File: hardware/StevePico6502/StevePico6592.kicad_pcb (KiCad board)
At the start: 2 copper layers, 112.4 x 101.6 mm, 29 parts, among them J1 Conn_01x16, J2 Conn_01x16, J3 Conn_02x16_Odd_Even, J4 Conn_01x01_Pin, SW1 SW_Push, SW2 SW_Push, U1 65CE02, U2 Pico, U3 74HC595, U4 W65C22NxP, U5 CY62256-70PC, U6 74HC00

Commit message: fixed bug with dual RAMSEL and no ROMSEL
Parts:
- U2: footprint Pi Pico:RPi_Pico_SMD_TH -> MCU_RaspberryPi_and_Boards:RPi_Pico_SMD_TH
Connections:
- U2 pad 10: /~{RAMSEL} -> /~{ROMSEL}
- U3 pad 13: /~{RAMSEL} -> /~{ROMSEL}
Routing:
- net /~{ROMSEL}: track 0.00 -> 52.0 mm, vias 0 -> 2
- net /~{RAMSEL}: track 120.1 -> 113.6 mm
- net /A14: track 135.2 -> 141.0 mm
- net /D1: track 155.2 -> 158.7 mm
- net /A7: track 159.9 -> 162.5 mm
- net GND: track 438.5 -> 440.5 mm
- net /~{IOSEL}: track 190.3 -> 191.5 mm
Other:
- board text added: "V082323 Has an error where GPIO5 and GPIO7 are both marked as ~{RAMSE}. To Fix: - cut the trace on the backside from pin 10 to the via which then connects to pin 7. - Pin 13 of U3 should be connected to ~{ROMSEL} not ~{RAMSEL} and will need to be cut and bodged. - Pin 20 of U5 should be connected to ~{RAMSE} with a bodge wire."

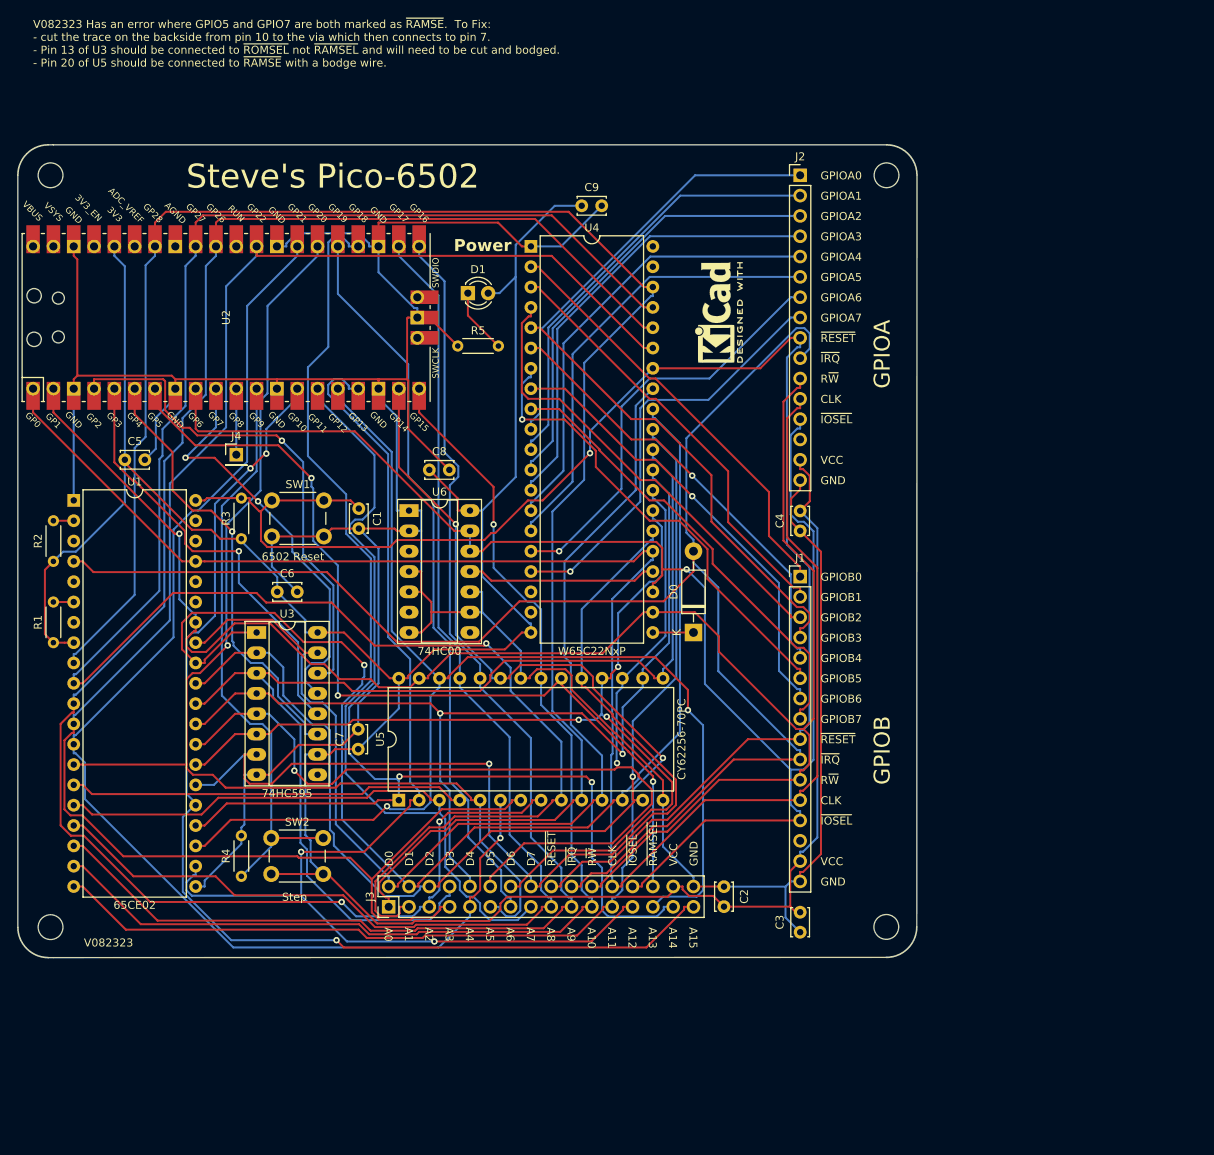
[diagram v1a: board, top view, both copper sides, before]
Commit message: V090323 - Removed Pico
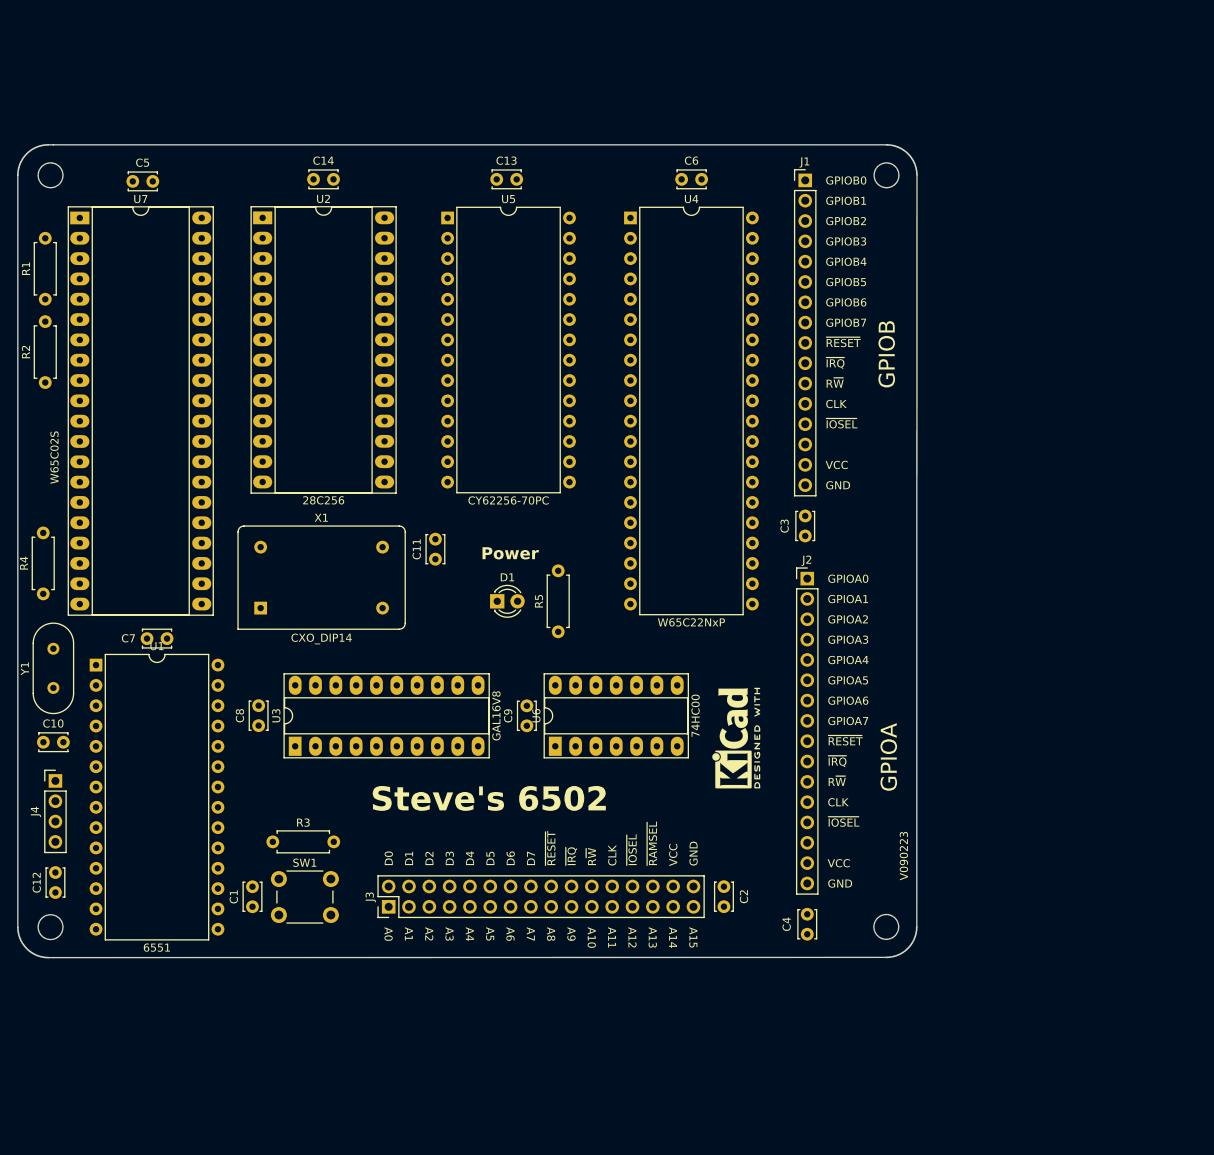
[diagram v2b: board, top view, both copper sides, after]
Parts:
- removed D0: SB140, Diode_THT:D_DO-41_SOD81_P10.16mm_Horizontal
- removed SW2: SW_Push, Button_Switch_THT:SW_PUSH_6mm
- added C10: 30pf, Capacitor_THT:C_Disc_D3.4mm_W2.1mm_P2.50mm, F.Cu at (52.1, 107.7)
- added C11: 1uF, Capacitor_THT:C_Disc_D3.4mm_W2.1mm_P2.50mm, F.Cu at (101.1, 84.8)
- added C12: 1uF, Capacitor_THT:C_Disc_D3.4mm_W2.1mm_P2.50mm, F.Cu at (53.6, 126.5)
- added C13: 1uF, Capacitor_THT:C_Disc_D3.4mm_W2.1mm_P2.50mm, F.Cu at (108.8, 37.3)
- added C14: 1uF, Capacitor_THT:C_Disc_D3.4mm_W2.1mm_P2.50mm, F.Cu at (85.9, 37.3)
- added U7: ~, Package_DIP:DIP-40_W15.24mm_Socket_LongPads, F.Cu at (56.6, 42.2)
- added X1: CXO_DIP14, Oscillator:Oscillator_DIP-14, F.Cu at (79.2, 90.9)
- added Y1: 1.8432, Crystal:Crystal_HC18-U_Vertical, F.Cu at (53.3, 100.9)
- J4: value Conn_01x01_Pin -> Conn_01x04; footprint Connector_PinHeader_2.54mm:PinHeader_1x01_P2.54mm_Vertical -> Connector_PinHeader_2.54mm:PinHeader_1x04_P2.54mm_Vertical
- R1, R2, R3, R4: footprint Resistor_THT:R_Axial_DIN0204_L3.6mm_D1.6mm_P5.08mm_Horizontal -> Resistor_THT:R_Axial_DIN0207_L6.3mm_D2.5mm_P7.62mm_Horizontal
- R5: value 1k -> 220; footprint Resistor_THT:R_Axial_DIN0204_L3.6mm_D1.6mm_P5.08mm_Horizontal -> Resistor_THT:R_Axial_DIN0207_L6.3mm_D2.5mm_P7.62mm_Horizontal
- U1: value 65CE02 -> 6551; footprint Package_DIP:DIP-40_W15.24mm -> Package_DIP:DIP-28_W15.24mm
- U2: value Pico -> 28C256; footprint MCU_RaspberryPi_and_Boards:RPi_Pico_SMD_TH -> Package_DIP:DIP-28_W15.24mm_Socket_LongPads
- U3: value 74HC595 -> GAL16V8; footprint Package_DIP:DIP-16_W7.62mm_Socket_LongPads -> Package_DIP:DIP-20_W7.62mm_Socket_LongPads
- moved U5 73.0 mm to (102.6, 42.2), turned to 0 degrees
- moved C6 72.2 mm to (131.9, 37.3)
- moved C9 65.4 mm to (112.5, 105.6), turned to 90 degrees
- moved REF** 53.3 mm to (138.7, 107.2)
- moved C1 51.5 mm to (78.2, 128.3), turned to 90 degrees
- moved C4 50.4 mm to (147.6, 129.2)
- moved J2 50.4 mm to (147.6, 87.2)
- moved J1 49.5 mm to (147.3, 37.5)
- moved C3 49.5 mm to (147.3, 79.4)
- moved SW1 47.3 mm to (81.5, 124.8)
- moved J4 46.6 mm to (53.6, 112.5)
- moved R4 43.1 mm to (52.1, 89.2)
- moved R1 42.9 mm to (52.3, 52.3)
- moved D1 38.7 mm to (108.8, 90.1)
- moved C8 38.4 mm to (79.0, 105.6), turned to 90 degrees
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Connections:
- J4 pad 1: Net-(J4-Pin_1) -> /RXD
- R1 pad 2: Net-(U1-~{NMI}) -> Net-(U7-RDY)
- R2 pad 2: Net-(U1-RDY) -> Net-(U7-NMIB)
- R4 pad 1: Net-(U2-GPIO9) -> Net-(U1-XTAL2)
- R4 pad 2: GND -> Net-(U1-XTAL1)
- U1 pad 10: /A1 -> /TXD
- U1 pad 11: /A2 -> unconnected-(U1-~{DTR}-Pad11)
- U1 pad 12: /A3 -> /RXD
- U1 pad 13: /A4 -> /A0
- U1 pad 14: /A5 -> /A1
- U1 pad 15: /A6 -> VCC
- U1 pad 16: /A7 -> unconnected-(U1-~{DCD}-Pad16)
- U1 pad 17: /A8 -> unconnected-(U1-~{DSR}-Pad17)
- U1 pad 18: /A9 -> /D0
- U1 pad 19: /A10 -> /D1
- U1 pad 2: Net-(U1-RDY) -> /UARTSEL
- U1 pad 20: /A11 -> /D2
- U1 pad 21: GND -> /D3
- U1 pad 22: /A12 -> /D4
- U1 pad 23: /A13 -> /D5
- U1 pad 24: /A14 -> /D6
- U1 pad 25: /A15 -> /D7
- U1 pad 26: /D7 -> unconnected-(U1-~{IRQ}-Pad26)
- U1 pad 27: /D6 -> /CLK
- U1 pad 28: /D5 -> /R~{W}
- U1 pad 3: unconnected-(U1-ϕ1-Pad3) -> /~{UARTSEL}
- U1 pad 4: /~{IRQ} -> /~{RESET}
- U1 pad 6: Net-(U1-~{NMI}) -> Net-(U1-XTAL1)
- U1 pad 7: unconnected-(U1-SYNC-Pad7) -> Net-(U1-XTAL2)
- U1 pad 8: VCC -> unconnected-(U1-~{RTS}-Pad8)
- U1 pad 9: /A0 -> unconnected-(U1-~{CTS}-Pad9)
- U2 pad 1: /CLK -> /A14
- U2 pad 10: /~{ROMSEL} -> /A0
- U2 pad 11: Net-(J4-Pin_1) -> /D0
- U2 pad 12: Net-(U2-GPIO9) -> /D1
- U2 pad 13: GND -> /D2
- U2 pad 14: /A15 -> GND
- U2 pad 15: /A14 -> /D3
- U2 pad 16: /A13 -> /D4
- U2 pad 17: /A12 -> /D5
- U2 pad 18: GND -> /D6
- U2 pad 19: /A11 -> /D7
- U2 pad 2: /R~{W} -> /A12
- U2 pad 20: /A10 -> /~{ROMSEL}
- U2 pad 21: /A9 -> /A10
- U2 pad 22: /A8 -> /R~{W}
- U2 pad 23: GND -> /A11
- U2 pad 24: /A7 -> /A9
- U2 pad 25: /A6 -> /A8
- U2 pad 26: /A5 -> /A13
- U2 pad 27: /A4 -> VCC
- U2 pad 28: GND -> VCC
- U2 pad 3: GND -> /A7
- U2 pad 4: Net-(U2-GPIO2) -> /A6
- U2 pad 5: Net-(U2-GPIO3) -> /A5
- U2 pad 6: Net-(U2-GPIO4) -> /A4
- U2 pad 7: /~{RAMSEL} -> /A3
- U2 pad 8: GND -> /A2
- U2 pad 9: /~{IOSEL} -> /A1
- U3 pad 1: /D1 -> /A15
- U3 pad 10: VCC -> GND
- U3 pad 11: Net-(U2-GPIO4) -> unconnected-(U3-I10/~{OE}-Pad11)
- U3 pad 12: Net-(U2-GPIO3) -> unconnected-(U3-IO8-Pad12)
- U3 pad 13: /~{ROMSEL} -> unconnected-(U3-IO7-Pad13)
- U3 pad 14: Net-(U2-GPIO2) -> unconnected-(U3-IO6-Pad14)
- U3 pad 15: /D0 -> unconnected-(U3-IO5-Pad15)
- U3 pad 16: VCC -> /~{UARTSEL}
- U3 pad 2: /D2 -> /A14
- U3 pad 3: /D3 -> /A13
- U3 pad 4: /D4 -> /A12
- U3 pad 5: /D5 -> /A11
- U3 pad 6: /D6 -> /A10
- U3 pad 7: /D7 -> /R~{W}
- U3 pad 8: GND -> /CLK
- U4 pad 21: Net-(D0-K) -> /~{IRQ}
- U6 pad 1: GND -> /~{UARTSEL}
- U6 pad 2: GND -> /~{UARTSEL}
- U6 pad 3: unconnected-(U6-Pad3) -> /UARTSEL
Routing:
- net GND: track 440.5 -> 0.00 mm
- net VCC: track 368.6 -> 0.00 mm
- net /A1: track 245.7 -> 0.00 mm, vias 1 -> 0
- net /A0: track 230.5 -> 0.00 mm
- net /A2: track 221.0 -> 0.00 mm, vias 2 -> 0
- net /R~{W}: track 220.3 -> 0.00 mm, vias 1 -> 0
- net /A3: track 216.1 -> 0.00 mm
- net /CLK: track 214.9 -> 0.00 mm
- net /~{RESET}: track 198.2 -> 0.00 mm, vias 1 -> 0
- net /~{IRQ}: track 194.4 -> 0.00 mm
- net /~{IOSEL}: track 191.5 -> 0.00 mm, vias 1 -> 0
- net /A7: track 162.5 -> 0.00 mm
- net /A11: track 162.2 -> 0.00 mm, vias 2 -> 0
- net /A9: track 159.6 -> 0.00 mm
- net /D1: track 158.7 -> 0.00 mm, vias 1 -> 0
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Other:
- board text added: "Steve's 6502"
- board text added: "V090223"
- board text added: "W65C02S"
- board text removed: "6502 Reset"
- board text removed: "Step"
- board text removed: "Steve's Pico-6502"
- board text removed: "V082323"
- board text removed: "V082323 Has an error where GPIO5 and GPIO7 are both marked as ~{RAMSE}. To Fix: - cut the trace on the backside from pin 10 to the via which then connects to pin 7. - Pin 13 of U3 should be connected to ~{ROMSEL} not ~{RAMSEL} and will need to be cut and bodged. - Pin 20 of U5 should be connected to ~{RAMSE} with a bodge wire."

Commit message: 6502 Rev 2
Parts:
- removed C11, C12, C13, C14: 1uF, Capacitor_THT:C_Disc_D3.4mm_W2.1mm_P2.50mm
- removed the C5 at (63.3, 37.6)
- removed J4: Conn_01x04, Connector_PinHeader_2.54mm:PinHeader_1x04_P2.54mm_Vertical
- removed R4: 1k, Resistor_THT:R_Axial_DIN0207_L6.3mm_D2.5mm_P7.62mm_Horizontal
- removed the REF** at (138.7, 107.2)
- removed U6: 74HC00, Package_DIP:DIP-14_W7.62mm_Socket_LongPads
- removed U7: ~, Package_DIP:DIP-40_W15.24mm_Socket_LongPads
- removed Y1: 1.8432, Crystal:Crystal_HC18-U_Vertical
- added C1: 1uF, Capacitor_THT:C_Disc_D3.4mm_W2.1mm_P2.50mm, F.Cu at (76.7, 97.8)
- added DS1: WC1602A, Display:WC1602A, F.Cu at (83.1, 119.4)
- added J6: Conn_02x11_Odd_Even, Connector_PinHeader_2.54mm:PinHeader_2x11_P2.54mm_Vertical, F.Cu at (101.9, 106.7)
- added REF**: KiCad-Logo2_6mm_SilkScreen, Symbol:KiCad-Logo2_6mm_SilkScreen, F.Cu at (61.5, 140.5)
- added RV1: 10k, Potentiometer_THT:Potentiometer_Bourns_3296W_Vertical, F.Cu at (163.8, 141.0)
- C10: value 30pf -> 1uF
- U1: value 6551 -> W65C02; footprint Package_DIP:DIP-28_W15.24mm -> Package_DIP:DIP-40_W15.24mm_Socket_LongPads
- U2: footprint Package_DIP:DIP-28_W15.24mm_Socket_LongPads -> Package_DIP:DIP-28_W15.24mm
- U3: value GAL16V8 -> CY62256-70PC; footprint Package_DIP:DIP-20_W7.62mm_Socket_LongPads -> Package_DIP:DIP-28_W15.24mm
- U4: value W65C22NxP -> W65C22S; footprint Package_DIP:DIP-40_W15.24mm -> Package_DIP:DIP-40_W15.24mm_Socket_LongPads
- U5: value CY62256-70PC -> 74HC00; footprint Package_DIP:DIP-28_W15.24mm -> Package_DIP:DIP-14_W7.62mm_Socket_LongPads
- moved C10 113.8 mm to (140.5, 36.1)
- moved C7 69.9 mm to (103.4, 36.3)
- moved C6 65.8 mm to (66.1, 36.3)
- moved R5 63.3 mm to (58.2, 118.6), turned to 0 degrees
- moved D1 59.7 mm to (61.0, 125.7)
- moved U1 57.2 mm to (59.7, 40.9)
- moved U5 49.4 mm to (110.7, 90.9), turned to 90 degrees
- moved C8 47.9 mm to (88.7, 58.7), turned to 0 degrees
- moved U3 31.1 mm to (88.4, 77.5)
- moved SW1 30.2 mm to (59.0, 104.6)
- moved C2 30.2 mm to (55.7, 108.1)
- moved R3 30.2 mm to (58.3, 100.0)
- moved J3 24.3 mm to (110.4, 109.2)
- moved C3 24.3 mm to (152.3, 109.2)
- moved X1 21.4 mm to (99.3, 83.6), turned to 180 degrees
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- renumbered C1 to C2, C2 to C3, C3 to C4, C4 to C5
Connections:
- C10 pad 1: Net-(U1-XTAL2) -> VCC
- R1 pad 2: Net-(U7-RDY) -> Net-(U1-RDY)
- R2 pad 2: Net-(U7-NMIB) -> Net-(U1-NMIB)
- U1 pad 1: GND -> unconnected-(U1-VPB-Pad1)
- U1 pad 10: /TXD -> /A1
- U1 pad 11: unconnected-(U1-~{DTR}-Pad11) -> /A2
- U1 pad 12: /RXD -> /A3
- U1 pad 13: /A0 -> /A4
- U1 pad 14: /A1 -> /A5
- U1 pad 15: VCC -> /A6
- U1 pad 16: unconnected-(U1-~{DCD}-Pad16) -> /A7
- U1 pad 17: unconnected-(U1-~{DSR}-Pad17) -> /A8
- U1 pad 18: /D0 -> /A9
- U1 pad 19: /D1 -> /A10
- U1 pad 2: /UARTSEL -> Net-(U1-RDY)
- U1 pad 20: /D2 -> /A11
- U1 pad 21: /D3 -> GND
- U1 pad 22: /D4 -> /A12
- U1 pad 23: /D5 -> /A13
- U1 pad 24: /D6 -> /A14
- U1 pad 25: /D7 -> /A15
- U1 pad 26: unconnected-(U1-~{IRQ}-Pad26) -> /D7
- U1 pad 27: /CLK -> /D6
- U1 pad 28: /R~{W} -> /D5
- U1 pad 3: /~{UARTSEL} -> unconnected-(U1-PHI1O-Pad3)
- U1 pad 4: /~{RESET} -> /~{IRQ}
- U1 pad 6: Net-(U1-XTAL1) -> Net-(U1-NMIB)
- U1 pad 7: Net-(U1-XTAL2) -> unconnected-(U1-SYNC-Pad7)
- U1 pad 8: unconnected-(U1-~{RTS}-Pad8) -> VCC
- U1 pad 9: unconnected-(U1-~{CTS}-Pad9) -> /A0
- U3 pad 1: /A15 -> /A14
- U3 pad 10: GND -> /A0
- U3 pad 11: unconnected-(U3-I10/~{OE}-Pad11) -> /D0
- U3 pad 12: unconnected-(U3-IO8-Pad12) -> /D1
- U3 pad 13: unconnected-(U3-IO7-Pad13) -> /D2
- U3 pad 14: unconnected-(U3-IO6-Pad14) -> GND
- U3 pad 15: unconnected-(U3-IO5-Pad15) -> /D3
- U3 pad 16: /~{UARTSEL} -> /D4
- U3 pad 17: /~{IOSEL} -> /D5
- U3 pad 18: /~{RAMSEL} -> /D6
- U3 pad 19: /~{ROMSEL} -> /D7
- U3 pad 2: /A14 -> /A12
- U3 pad 20: VCC -> /~{RAMSEL}
- U3 pad 3: /A13 -> /A7
- U3 pad 4: /A12 -> /A6
- U3 pad 5: /A11 -> /A5
- U3 pad 6: /A10 -> /A4
- U3 pad 7: /R~{W} -> /A3
- U3 pad 8: /CLK -> /A2
- U3 pad 9: unconnected-(U3-I9-Pad9) -> /A1
- U4 pad 10: /GPIOA0 -> /GPIOB0
- U4 pad 11: /GPIOA1 -> /GPIOB1
- U4 pad 12: /GPIOA2 -> /GPIOB2
- U4 pad 13: /GPIOA3 -> /GPIOB3
- U4 pad 14: /GPIOA4 -> /GPIOB4
- U4 pad 15: /GPIOA5 -> /GPIOB5
- U4 pad 16: /GPIOA6 -> /GPIOB6
- U4 pad 17: /GPIOA7 -> /GPIOB7
- U4 pad 2: /GPIOB0 -> /GPIOA0
- U4 pad 24: /IOSEL -> /A13
- U4 pad 3: /GPIOB1 -> /GPIOA1
- U4 pad 4: /GPIOB2 -> /GPIOA2
- U4 pad 5: /GPIOB3 -> /GPIOA3
- U4 pad 6: /GPIOB4 -> /GPIOA4
- U4 pad 7: /GPIOB5 -> /GPIOA5
- U4 pad 8: /GPIOB6 -> /GPIOA6
- U4 pad 9: /GPIOB7 -> /GPIOA7
- U5 pad 1: /A14 -> /A15
- U5 pad 10: /A0 -> /A14
- U5 pad 11: /D0 -> unconnected-(U5-Pad11)
- U5 pad 12: /D1 -> GND
- U5 pad 13: /D2 -> GND
- U5 pad 14: GND -> VCC
- U5 pad 2: /A12 -> /A15
- U5 pad 3: /A7 -> /~{ROMSEL}
- U5 pad 4: /A6 -> /~{ROMSEL}
- U5 pad 5: /A5 -> /CLK
- U5 pad 6: /A4 -> /~{RAMSEL}
- U5 pad 7: /A3 -> GND
- U5 pad 8: /A2 -> /~{IOSEL}
- U5 pad 9: /A1 -> /~{ROMSEL}
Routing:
- net VCC: track 0.00 -> 489.1 mm, vias 0 -> 1
- net GND: track 0.00 -> 461.3 mm, vias 0 -> 1
- net /~{RESET}: track 0.00 -> 253.4 mm
- net /R~{W}: track 0.00 -> 239.9 mm, vias 0 -> 3
- net /~{IRQ}: track 0.00 -> 230.3 mm, vias 0 -> 1
- net /CLK: track 0.00 -> 200.2 mm, vias 0 -> 1
- net /A11: track 0.00 -> 198.7 mm, vias 0 -> 1
- net /A3: track 0.00 -> 185.8 mm, vias 0 -> 2
- net /GPIOA5: track 0.00 -> 181.5 mm
- net /A2: track 0.00 -> 167.7 mm, vias 0 -> 1
- net /A13: track 0.00 -> 167.7 mm, vias 0 -> 2
- net /D2: track 0.00 -> 163.5 mm, vias 0 -> 1
- net /A0: track 0.00 -> 160.2 mm
- net /A1: track 0.00 -> 158.8 mm, vias 0 -> 1
- net /D4: track 0.00 -> 156.0 mm, vias 0 -> 1
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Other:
- board size 112.4 x 101.6 mm -> 128.4 x 124 mm
- board text added: "LCD Enable"
- board text added: "Reset"
- board text removed: "W65C02S"

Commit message: V090423
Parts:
- added J4: Conn_01x02_Pin, Connector_PinHeader_2.54mm:PinHeader_1x02_P2.54mm_Vertical, F.Cu at (162.3, 141.0)
- added J5: Conn_01x02_Pin, Connector_PinHeader_2.54mm:PinHeader_1x02_P2.54mm_Vertical, F.Cu at (162.3, 137.2)
- added J7: Conn_01x02_Pin, Connector_PinHeader_2.54mm:PinHeader_1x02_P2.54mm_Vertical, F.Cu at (162.3, 144.8)
- U1: value W65C02 -> W65C02S
- moved RV1 99.2 mm to (64.8, 135.6), turned to 0 degrees
- moved J6 25.8 mm to (76.2, 109.2), turned to 90 degrees
- moved C7 23.6 mm to (83.6, 49.0), turned to 90 degrees
- moved X1 15.9 mm to (85.3, 91.2), turned to 0 degrees
- moved C8 13.2 mm to (83.6, 70.8), turned to 90 degrees
- moved C1 9.83 mm to (80.3, 88.6)
- moved REF** 6.41 mm to (62.7, 146.8)
- moved R3 4.76 mm to (58.4, 95.2)
- moved D1 4.57 mm to (61.0, 121.2)
- moved SW1 4.54 mm to (59.0, 100.1)
- moved C2 4.51 mm to (55.4, 103.6)
- moved R5 4.33 mm to (58.4, 114.3)
- moved C3 3.44 mm to (155.7, 108.9)
- moved J3 3.17 mm to (113.5, 109.2)
- moved C4 2.37 mm to (163.6, 81.8), turned to 90 degrees
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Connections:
- U2 pad 22: /R~{W} -> GND
- U3 pad 22: GND -> /A14
- U5 pad 3: /~{ROMSEL} -> /~{ROMSEL_INT}
- U5 pad 4: /~{ROMSEL} -> /~{ROMSEL_INT}
- U5 pad 6: /~{RAMSEL} -> /~{RAMSEL_INT}
- U5 pad 8: /~{IOSEL} -> /~{IOSEL_INT}
- U5 pad 9: /~{ROMSEL} -> /~{ROMSEL_INT}
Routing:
- net /~{ROMSEL_INT}: track 0.00 -> 105.0 mm, vias 0 -> 3
- net /~{ROMSEL}: track 76.2 -> 167.3 mm, vias 0 -> 1
- net /~{IOSEL_INT}: track 0.00 -> 90.2 mm
- net /~{RAMSEL_INT}: track 0.00 -> 83.8 mm
- net /GPIOA5: track 181.5 -> 118.9 mm, vias 0 -> 1
- net Net-(DS1-VO): track 85.7 -> 33.1 mm
- net /~{RAMSEL}: track 73.1 -> 122.2 mm
- net /A11: track 198.7 -> 158.2 mm, vias 1 -> 2
- net /A10: track 151.6 -> 189.0 mm, vias 2 -> 1
- net /D1: track 139.0 -> 173.8 mm, vias 1 -> 3
- net /GPIOB0: track 108.8 -> 141.0 mm
- net /A9: track 155.3 -> 184.8 mm, vias 2 -> 0
- net /R~{W}: track 239.9 -> 211.6 mm, vias 3 -> 1
- net /GPIOB2: track 110.5 -> 135.6 mm
- net /GPIOA7: track 133.6 -> 110.2 mm, vias 2 -> 1
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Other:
- board text added: "Connect to use internal glue logic"
- board text added: "Jumper to connect LCD to GPIOB and the 3 highest bits of GPIOA"
- board text added: "V090423"
- board text added: "~{ROMSEL}"
- board text removed: "V090223"
